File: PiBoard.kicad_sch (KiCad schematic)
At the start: 8 parts

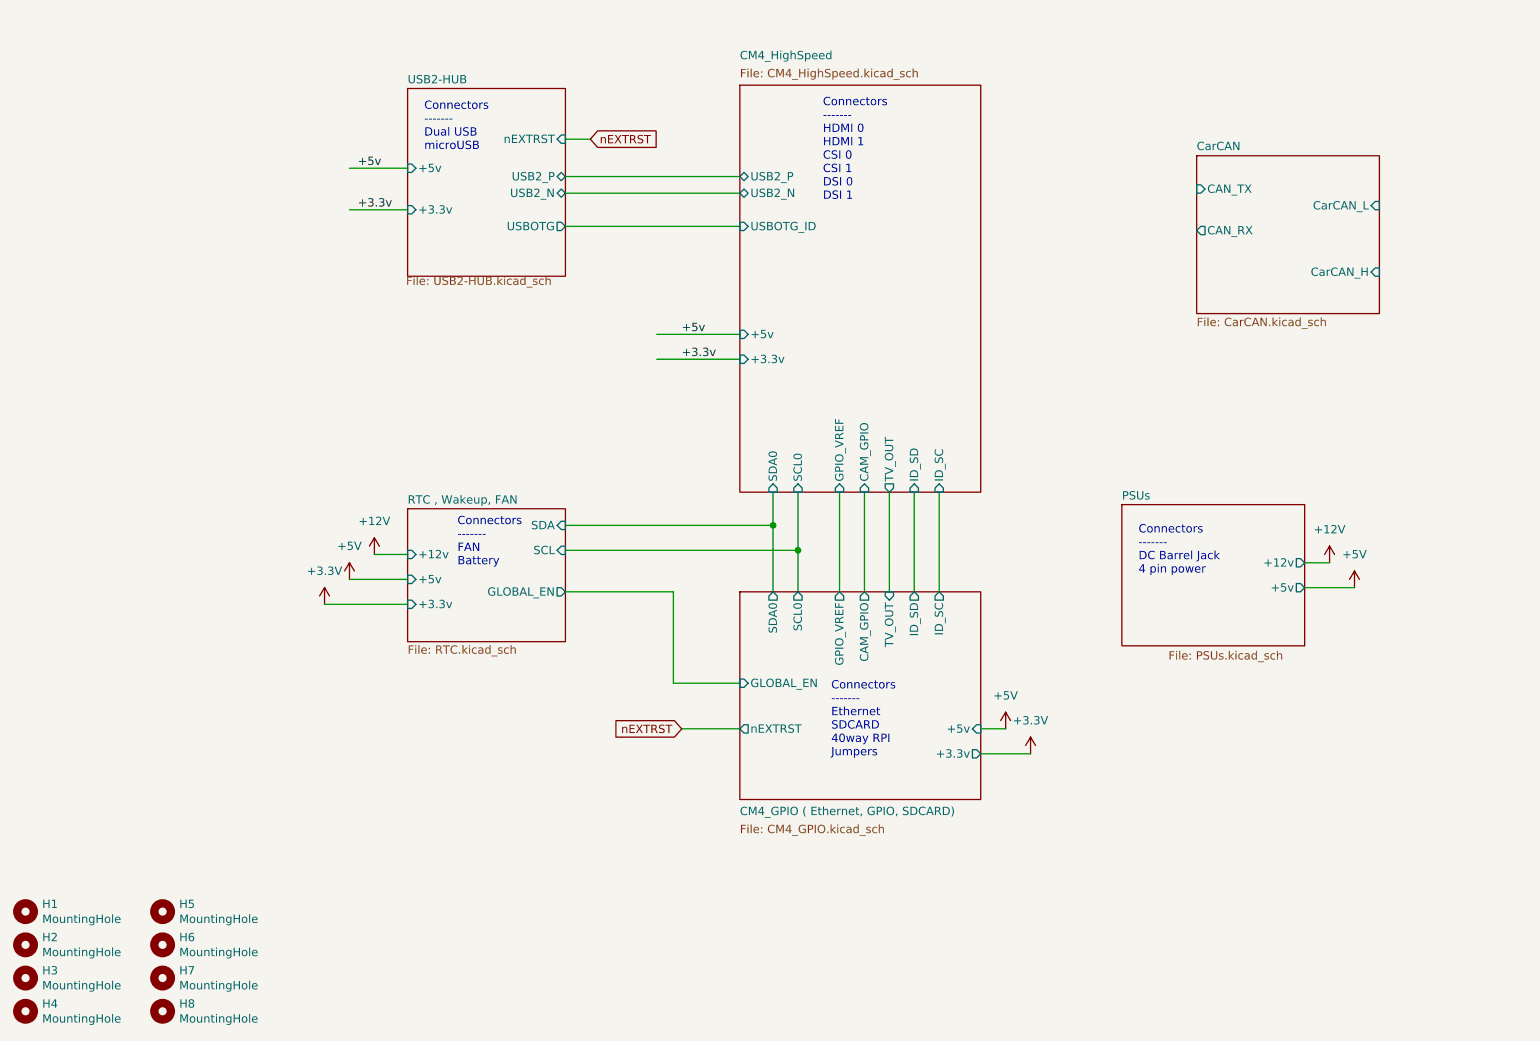
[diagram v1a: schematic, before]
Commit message: power dist, hdmi, and rtc are done; finding a new usb hub
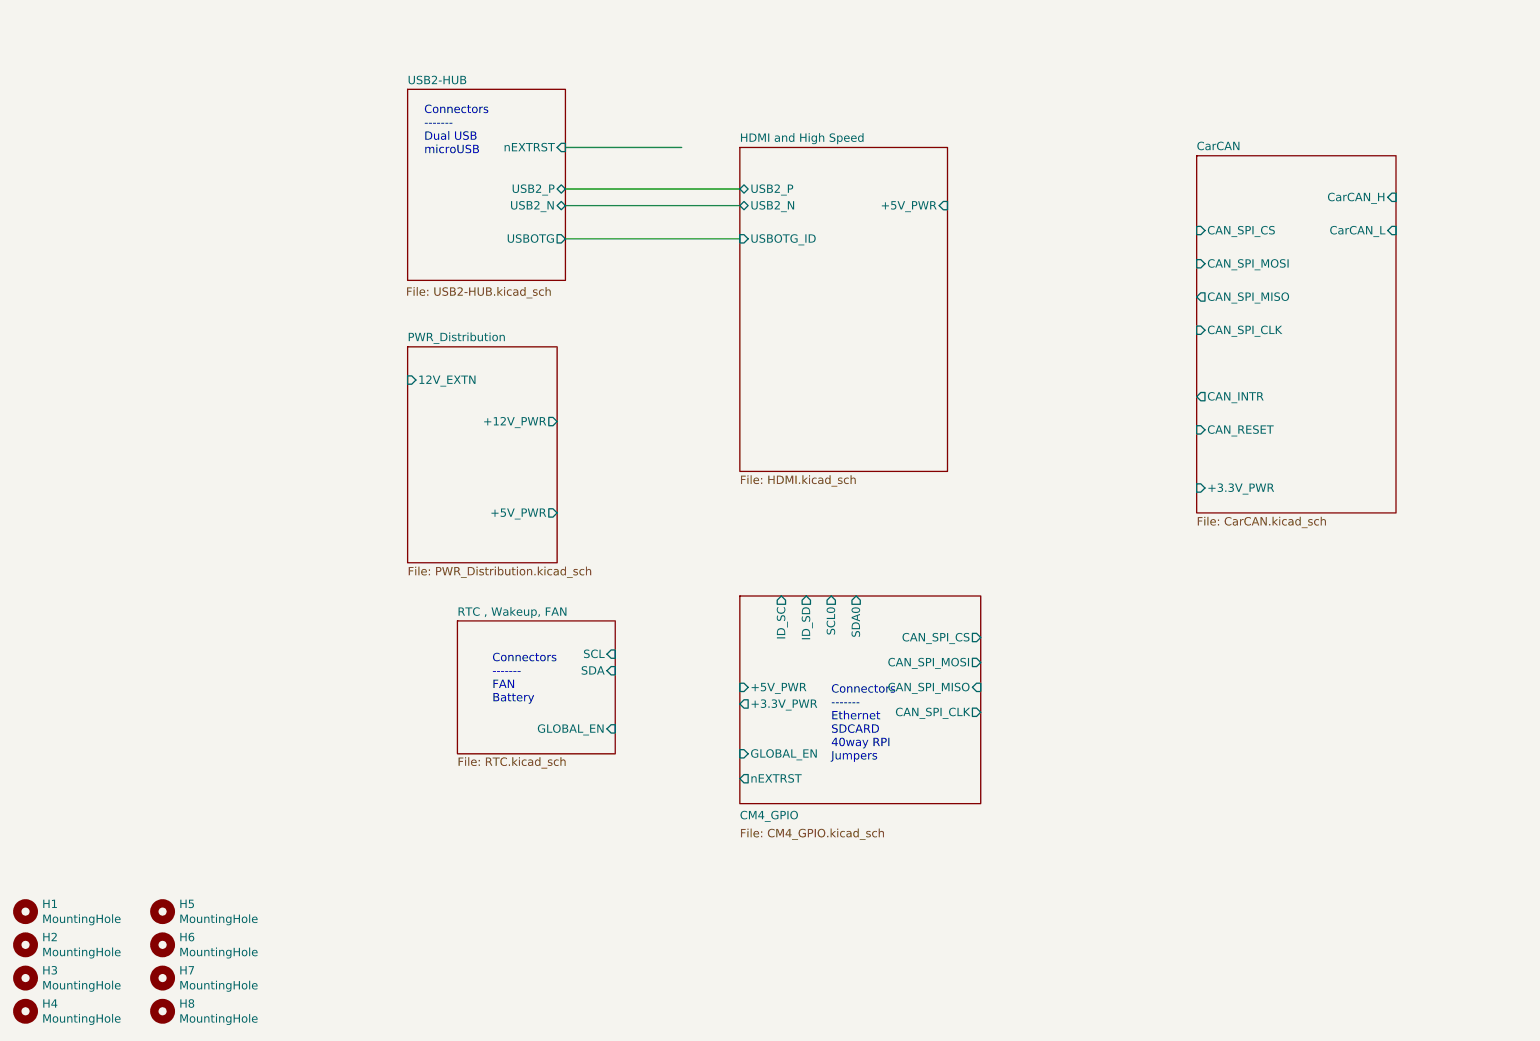
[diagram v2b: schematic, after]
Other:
- sheet CM4_GPIO ( Ethernet, GPIO, SDCARD) renamed CM4_GPIO
- removed sheet CM4_HighSpeed
- removed sheet PSUs
- added sheet HDMI and High Speed (HDMI.kicad_sch)
- added sheet PWR_Distribution (PWR_Distribution.kicad_sch)
- sheet CM4_GPIO ports: added +3.3V_PWR, +5V_PWR, CAN_SPI_CLK, CAN_SPI_CS, CAN_SPI_MISO, CAN_SPI_MOSI; removed +3.3v, +5v, CAM_GPIO, GPIO_VREF, TV_OUT
- sheet CarCAN ports: added +3.3V_PWR, CAN_INTR, CAN_RESET, CAN_SPI_CLK, CAN_SPI_CS, CAN_SPI_MISO, CAN_SPI_MOSI; removed CAN_RX, CAN_TX
- sheet RTC , Wakeup, FAN ports: added none; removed +12v, +3.3v, +5v
- sheet USB2-HUB ports: added none; removed +3.3v, +5v
- note removed: "Connectors ------- DC Barrel Jack 4 pin power"
- note removed: "Connectors ------- HDMI 0 HDMI 1 CSI 0 CSI 1 DSI 0 DSI 1"

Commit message: made more changes
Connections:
- no-connect marks 0 -> 4
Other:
- sheet USB2-HUB ports: added +3.3V_PWR, +5V_PWR; removed nEXTRST
- note added: "Connectors ------- 4x USB (M8 port) microUSB"
- note added: "Connectors ------- SDCARD 40way RPI Jumpers"
- note removed: "Connectors ------- Dual USB microUSB"
- note removed: "Connectors ------- Ethernet SDCARD 40way RPI Jumpers"

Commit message: finished USB i think, working on general gpio in more detail
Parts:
- removed H1, H2, H3, H4, H5, H6, H7, H8: MountingHole, MountingHole:MountingHole_2.7mm_M2.5, symbol Mechanical:MountingHole
- added J2: CANConnector, UTSVT_Connectors:Molex_MicroFit3.0_1x4xP3.00mm_PolarizingPeg_Vertical, symbol utsvt-connectors:CANConnector
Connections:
- net CarCAN/CarCAN_H: now also J2.3 (CAN_H)
- net CarCAN/CarCAN_L: now also J2.4 (CAN_L)
- no-connect marks 4 -> 5
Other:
- sheet PWR_Distribution ports: added none; removed 12V_EXTN
- sheet RTC , Wakeup, FAN ports: added +12V_PWR, +3.3V_PWR, +5V_PWR; removed none

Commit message: random stuff before i screw with my windows install
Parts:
- removed J2: CANConnector, UTSVT_Connectors:Molex_MicroFit3.0_1x4xP3.00mm_PolarizingPeg_Vertical, symbol utsvt-connectors:CANConnector
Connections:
- no-connect marks 5 -> 3
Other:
- sheet CM4_GPIO ports: added +3.3V_PWR_1, +3.3V_PWR_2; removed +3.3V_PWR
- sheet CarCAN ports: added none; removed CarCAN_H, CarCAN_L
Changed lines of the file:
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@@
-	)
-	(junction
-		(at 128.27 135.89)
-		(diameter 0)
-		(color 0 0 0 0)
 	)
 	(junction
@@
 		(color 0 0 0 0)
 	)
-	(no_connect
-		(at 222.25 100.33)
+	(junction
+		(at 128.27 129.54)
+		(diameter 0)
+		(color 0 0 0 0)
 	)
 	(no_connect
@@
 	)
 	(no_connect
-		(at 222.25 97.79)
-	)
-	(no_connect
 		(at 140.97 88.9)
 	)
@@
 	(wire
 		(pts
-			(xy 120.65 151.13) (xy 120.65 83.82)
+			(xy 120.65 144.78) (xy 120.65 83.82)
 		)
 		(stroke
@@
 	(wire
 		(pts
-			(xy 125.73 158.75) (xy 125.73 111.76)
-		)
-		(stroke
-			(width 0)
-			(type default)
-		)
-	)
-	(wire
-		(pts
-			(xy 86.36 134.62) (xy 86.36 116.84)
+			(xy 125.73 152.4) (xy 125.73 111.76)
+		)
+		(stroke
+			(width 0)
+			(type default)
+		)
+	)
+	(wire
+		(pts
+			(xy 86.36 128.27) (xy 86.36 116.84)
 		)
 		(stroke
@@
 	(wire
 		(pts
-			(xy 115.57 158.75) (xy 125.73 158.75)
+			(xy 115.57 152.4) (xy 125.73 152.4)
 		)
 		(stroke
@@
 	(wire
 		(pts
-			(xy 83.82 137.16) (xy 83.82 114.3)
+			(xy 83.82 130.81) (xy 83.82 114.3)
 		)
 		(stroke
@@
 	(wire
 		(pts
-			(xy 123.19 153.67) (xy 123.19 86.36)
-		)
-		(stroke
-			(width 0)
-			(type default)
-		)
-	)
-	(wire
-		(pts
-			(xy 91.44 134.62) (xy 86.36 134.62)
-		)
-		(stroke
-			(width 0)
-			(type default)
-		)
-	)
-	(wire
-		(pts
-			(xy 128.27 105.41) (xy 128.27 135.89)
+			(xy 123.19 147.32) (xy 123.19 86.36)
+		)
+		(stroke
+			(width 0)
+			(type default)
+		)
+	)
+	(wire
+		(pts
+			(xy 91.44 128.27) (xy 86.36 128.27)
+		)
+		(stroke
+			(width 0)
+			(type default)
+		)
+	)
+	(wire
+		(pts
+			(xy 128.27 105.41) (xy 128.27 129.54)
 		)
 		(stroke
@@
 	(wire
 		(pts
-			(xy 177.8 135.89) (xy 128.27 135.89)
-		)
-		(stroke
-			(width 0)
-			(type default)
-		)
-	)
-	(wire
-		(pts
-			(xy 115.57 153.67) (xy 123.19 153.67)
+			(xy 177.8 129.54) (xy 128.27 129.54)
+		)
+		(stroke
+			(width 0)
+			(type default)
+		)
+	)
+	(wire
+		(pts
+			(xy 115.57 147.32) (xy 123.19 147.32)
 		)
 		(stroke
@@
 	(wire
 		(pts
-			(xy 115.57 135.89) (xy 128.27 135.89)
-		)
-		(stroke
-			(width 0)
-			(type default)
-		)
-	)
-	(wire
-		(pts
-			(xy 208.28 95.25) (xy 222.25 95.25)
-		)
-		(stroke
-			(width 0)
-			(type default)
-		)
-	)
-	(wire
-		(pts
-			(xy 115.57 151.13) (xy 120.65 151.13)
+			(xy 115.57 129.54) (xy 128.27 129.54)
+		)
+		(stroke
+			(width 0)
+			(type default)
+		)
+	)
+	(wire
+		(pts
+			(xy 115.57 144.78) (xy 120.65 144.78)
 		)
 		(stroke
@@
 	(wire
 		(pts
-			(xy 208.28 92.71) (xy 222.25 92.71)
-		)
-		(stroke
-			(width 0)
-			(type default)
-		)
-	)
-	(wire
-		(pts
-			(xy 91.44 137.16) (xy 83.82 137.16)
+			(xy 91.44 130.81) (xy 83.82 130.81)
 		)
 		(stroke
@@
 		)
 	)
-	(symbol
-		(lib_id "utsvt-connectors:CANConnector")
-		(at 231.14 96.52 180)
-		(unit 1)
-		(exclude_from_sim no)
-		(in_bom yes)
-		(on_board yes)
-		(dnp no)
-		(fields_autoplaced yes)
-		(property "Reference" "J2"
-			(at 236.22 95.2499 0)
-			(effects
-				(font
-					(size 1.524 1.524)
-				)
-				(justify right)
-			)
-		)
-		(property "Value" "CANConnector"
-			(at 236.22 97.7899 0)
-			(effects
-				(font
-					(size 1.524 1.524)
-				)
-				(justify right)
-			)
-		)
-		(property "Footprint" "UTSVT_Connectors:Molex_MicroFit3.0_1x4xP3.00mm_PolarizingPeg_Vertical"
-			(at 231.14 87.63 0)
-			(effects
-				(font
-					(size 1.524 1.524)
-				)
-				(hide yes)
-			)
-		)
-		(property "Datasheet" ""
-			(at 227.33 104.14 0)
-			(effects
-				(font
-					(size 1.524 1.524)
-				)
-				(hide yes)
-			)
-		)
-		(property "Description" "Connection to the car's CAN bus."
-			(at 231.14 96.52 0)
-			(effects
-				(font
-					(size 1.27 1.27)
-				)
-				(hide yes)
-			)
-		)
-		(pin "2"
-		)
-		(pin "3"
-		)
-		(pin "1"
-		)
-		(pin "4"
-		)
-		(instances
-			(project ""
-				(path "/e4d65698-b8ec-4bf6-9f2b-a5010377155a"
-					(reference "J2")
-					(unit 1)
-				)
-			)
-		)
-	)
 	(sheet
 		(at 82.55 77.47)
@@
 			)
 		)
-		(pin "+3.3V_PWR" output
-			(at 134.62 105.41 180)
-			(effects
-				(font
-					(size 1.27 1.27)
-				)
-				(justify left)
-			)
-		)
 		(pin "GLOBAL_EN" input
 			(at 134.62 111.76 180)
@@
 		(pin "nEXTRST" output
 			(at 134.62 115.57 180)
+			(effects
+				(font
+					(size 1.27 1.27)
+				)
+				(justify left)
+			)
+		)
+		(pin "+3.3V_PWR_2" output
+			(at 171.45 116.84 0)
+			(effects
+				(font
+					(size 1.27 1.27)
+				)
+				(justify right)
+			)
+		)
+		(pin "+3.3V_PWR_1" output
+			(at 134.62 105.41 180)
 			(effects
 				(font
@@
 	)
 	(sheet
-		(at 91.44 129.54)
+		(at 91.44 123.19)
 		(size 24.13 31.75)
 		(stroke
@@
 		)
 		(property "Sheetname" "RTC , Wakeup, FAN"
-			(at 91.44 128.9045 0)
+			(at 91.44 122.5545 0)
 			(effects
 				(font
@@
 		)
 		(property "Sheetfile" "RTC.kicad_sch"
-			(at 92.456 162.306 0)
+			(at 92.456 155.956 0)
 			(effects
 				(font
@@
 		)
 		(pin "SCL" input
-			(at 115.57 151.13 0)
+			(at 115.57 144.78 0)
 			(effects
 				(font
@@
 		)
 		(pin "SDA" input
-			(at 115.57 153.67 0)
+			(at 115.57 147.32 0)
 			(effects
 				(font
@@
 		)
 		(pin "GLOBAL_EN" input
-			(at 115.57 158.75 0)
+			(at 115.57 152.4 0)
 			(effects
 				(font
@@
 		)
 		(pin "+3.3V_PWR" input
-			(at 115.57 135.89 0)
+			(at 115.57 129.54 0)
 			(effects
 				(font
@@
 		)
 		(pin "+5V_PWR" input
-			(at 91.44 134.62 180)
+			(at 91.44 128.27 180)
 			(effects
 				(font
@@
 		)
 		(pin "+12V_PWR" input
-			(at 91.44 137.16 180)
+			(at 91.44 130.81 180)
 			(effects
 				(font
@@
 	(sheet
 		(at 177.8 85.09)
-		(size 30.48 54.61)
+		(size 24.13 46.99)
 		(fields_autoplaced yes)
 		(stroke
@@
 		)
 		(property "Sheetfile" "CarCAN.kicad_sch"
-			(at 177.8 140.2846 0)
+			(at 177.8 132.6646 0)
 			(effects
 				(font
@@
 		)
 		(pin "+3.3V_PWR" input
-			(at 177.8 135.89 180)
+			(at 177.8 129.54 180)
 			(effects
 				(font
@@
 			)
 		)
-		(pin "CarCAN_L" input
-			(at 208.28 92.71 0)
-			(effects
-				(font
-					(size 1.27 1.27)
-				)
-				(justify right)
-			)
-		)
-		(pin "CarCAN_H" input
-			(at 208.28 95.25 0)
-			(effects
-				(font
-					(size 1.27 1.27)
-				)
-				(justify right)
-			)
-		)

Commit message: we ballin??
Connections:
- no-connect marks 3 -> 0
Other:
- sheet CM4_GPIO renamed CM4 GPIO
- sheet PWR_Distribution renamed Power Distribution
- sheet RTC , Wakeup, FAN renamed RTC and Fan
- sheet USB2-HUB renamed USB2.0 HS Hub
- sheet CM4 GPIO ports: added +3.3V_PWR, CAN_INTR; removed +3.3V_PWR_1, +3.3V_PWR_2, ID_SC, ID_SD
- note added: "Connectors ------- 40way RPI Jumpers"
- note added: "Connectors ------- HDMI (type E) port"
- note removed: "Connectors ------- SDCARD 40way RPI Jumpers"
